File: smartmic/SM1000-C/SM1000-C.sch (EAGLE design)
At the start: 177 parts, among them CN1 HDR100-3, CN10 MJ-3523-SMT, CN11 HDR100-3, CN12 DF11-16DS, CN2 MOLEX-MINI-B-SMT, CN3 RASM712PX, CN4 RJ-45, CN5 MJ-3523-SMT, CN6 MJ-3523-SMT, CN7 MJ-3523-SMT, CN8 MJ-3523-SMT, CN9 MJ-3523-SMT, J1 JMP-2PIN, J3 JMP-2PIN, J4 JMP-2PIN, J5 JMP-2PIN, P1 TPAD50, P10 TPAD50, P11 TPAD50, P12 TPAD50, P13 TPAD50, P14 TPAD50, P15 TPAD50, P16 TPAD50, P17 TPAD50, P18 TPAD50, P19 TPAD50, P2 TPAD50, P20 TPAD50, P3 TPAD50, P4 TPAD50, P5 TPAD50, P6 TPAD50, P7 TPAD50, P8 TPAD50, P9 TPAD50, SW1 SW-BOURNS-7914S, SW2 SW-BOURNS-7914S, SW3 DPDT, SW4 SW-BOURNS-7914S, T1 SM-LP-5001, T2 SM-LP-5001, U1 STM32F405, U2 LD3985M33R, U3 STMPS2141, U4 EMIF02-USB03F2, U5 TPS54329E, U6 LMV341, U7 LMV341, U8 LM386M-1, U9 LMV341

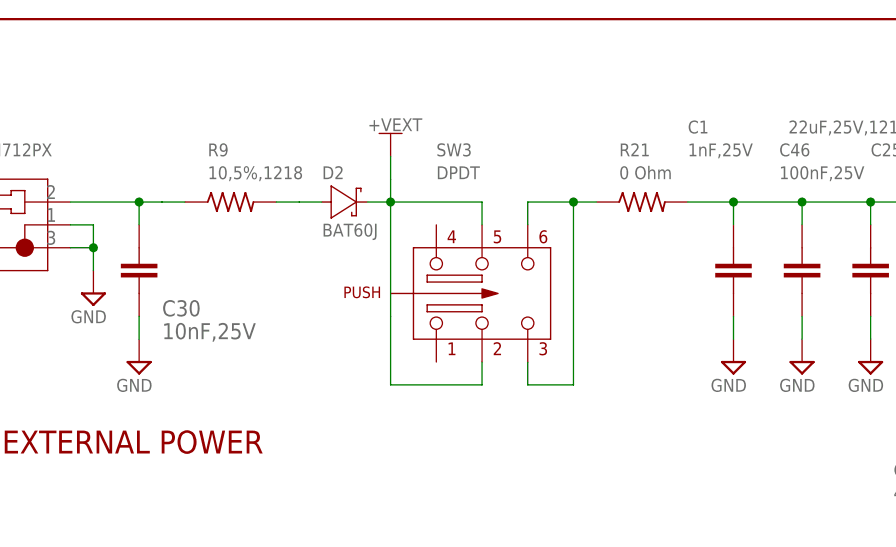
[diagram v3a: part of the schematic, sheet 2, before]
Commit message: Update Change-Log-C.txt #53 & #55  RGB 09/11/2014
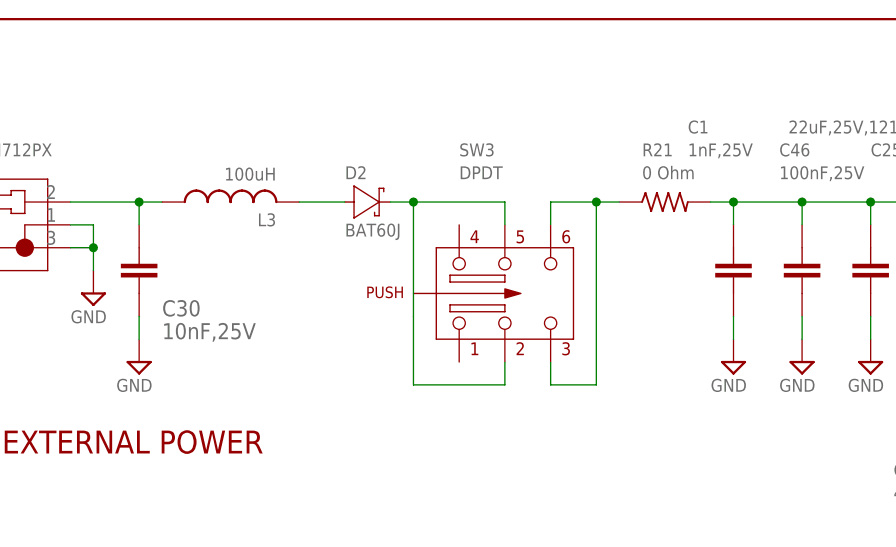
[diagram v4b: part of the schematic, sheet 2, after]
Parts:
- removed R9: 10,5%,1218, SM1000:RCL1218
- added L3: 100uH, _RoweTel:CBC3225T101MR
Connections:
- net +VEXT renamed N$15
- net N$24: now also L3.2; no longer R9.2
- net N$77: now also L3.1; no longer R9.1
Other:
- moved on the sheet: D2, R21, SW3
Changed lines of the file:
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@@
 <part name="V110" library="A-SUPPLY2" deviceset="GND" device=""/>
 <part name="U$1" library="A-SUPPLY2" deviceset="+VIN" device=""/>
-<part name="U$7" library="A-SUPPLY2" deviceset="+VEXT" device=""/>
 <part name="V71" library="A-SUPPLY2" deviceset="GND" device=""/>
 <part name="C52" library="AA-ipc-7351-capacitor" deviceset="CAPACITOR_" device="0603" value="100nF,16V"/>
@@
 <part name="C30" library="AA-ipc-7351-capacitor" deviceset="CAPACITOR_" device="0603" value="10nF,25V"/>
 <part name="V122" library="A-SUPPLY2" deviceset="GND" device=""/>
-<part name="R9" library="SM1000" deviceset="RCL1218" device="" value="10,5%,1218"/>
 <part name="R11" library="AA-ipc-7351-resistor" deviceset="RESISTOR_" device="0603" value="100,1%"/>
 <part name="R18" library="_RoweTel" deviceset="RES0805" device="" value="0 Ohm"/>
@@
 <part name="C54" library="AA-ipc-7351-capacitor" deviceset="CAPACITOR_" device="0603" value="1nF,16V"/>
 <part name="R23" library="AA-ipc-7351-resistor" deviceset="RESISTOR_" device="0603" value="10K,1%"/>
+<part name="L3" library="_RoweTel" deviceset="CBC3225T101MR" device="" value="100uH"/>
 </parts>
 <sheets>
@@
 <attribute name="VALUE" x="40.64" y="60.96" size="1.4224" layer="96" ratio="9" rot="MR270"/>
 </instance>
-<instance part="SW3" gate="G$1" x="73.66" y="248.92" smashed="yes" rot="MR0">
-<attribute name="NAME" x="68.58" y="264.16" size="1.4224" layer="95" ratio="10"/>
-<attribute name="VALUE" x="68.58" y="261.62" size="1.4224" layer="96" ratio="10"/>
+<instance part="SW3" gate="G$1" x="76.2" y="248.92" smashed="yes" rot="MR0">
+<attribute name="NAME" x="71.12" y="264.16" size="1.4224" layer="95" ratio="10"/>
+<attribute name="VALUE" x="71.12" y="261.62" size="1.4224" layer="96" ratio="10"/>
 </instance>
 <instance part="C26" gate="G$1" x="177.8" y="254" smashed="yes" rot="R270">
@@
 <attribute name="VALUE" x="106.68" y="237.998" size="1.4224" layer="96" ratio="9"/>
 </instance>
-<instance part="D2" gate="G$1" x="58.42" y="259.08" smashed="yes" rot="R180">
-<attribute name="NAME" x="55.88" y="261.62" size="1.4224" layer="95" ratio="10"/>
-<attribute name="VALUE" x="55.88" y="255.2446" size="1.4224" layer="96" ratio="10"/>
+<instance part="D2" gate="G$1" x="60.96" y="259.08" smashed="yes" rot="R180">
+<attribute name="NAME" x="58.42" y="261.62" size="1.4224" layer="95" ratio="10"/>
+<attribute name="VALUE" x="58.42" y="255.2446" size="1.4224" layer="96" ratio="10"/>
 </instance>
 <instance part="MIC1" gate="G$1" x="35.56" y="172.72" smashed="yes">
@@
 <attribute name="VALUE" x="121.92" y="267.208" size="1.4224" layer="95" ratio="9"/>
 </instance>
-<instance part="U$7" gate="G$1" x="63.5" y="266.7" smashed="yes">
-<attribute name="VALUE" x="60.96" y="266.954" size="1.4224" layer="96" ratio="9"/>
-</instance>
 <instance part="V17" gate="G$1" x="76.2" y="165.1" smashed="yes">
 <attribute name="VALUE" x="73.66" y="168.148" size="1.4224" layer="95" ratio="9"/>
@@
 <attribute name="VALUE" x="33.02" y="237.998" size="1.4224" layer="96" ratio="9"/>
 </instance>
-<instance part="R9" gate="G$1" x="45.72" y="259.08"/>
 <instance part="R11" gate="G$1" x="66.04" y="132.08" smashed="yes">
 <attribute name="NAME" x="63.5" y="133.604" size="1.4224" layer="95"/>
 <attribute name="VALUE" x="63.5" y="128.778" size="1.4224" layer="96"/>
 </instance>
-<instance part="R21" gate="G$1" x="91.44" y="259.08"/>
+<instance part="R21" gate="G$1" x="93.98" y="259.08"/>
 <instance part="R22" gate="G$1" x="27.94" y="60.96" smashed="yes" rot="R90">
 <attribute name="NAME" x="22.86" y="58.42" size="1.4224" layer="95" ratio="9" rot="R90"/>
@@
 <attribute name="VALUE" x="187.96" y="149.86" size="1.4224" layer="96" ratio="9"/>
 </instance>
+<instance part="L3" gate="G$1" x="45.72" y="259.08" smashed="yes" rot="R90">
+<attribute name="NAME" x="50.8" y="257.81" size="1.4224" layer="95" rot="R180"/>
+<attribute name="VALUE" x="50.8" y="262.89" size="1.4224" layer="96" rot="R180"/>
+</instance>
 </instances>
 <busses>
@@
 <wire x1="109.22" y1="256.54" x2="109.22" y2="259.08" width="0.1524" layer="91"/>
 <junction x="109.22" y="259.08"/>
-<wire x1="96.52" y1="259.08" x2="101.6" y2="259.08" width="0.1524" layer="91"/>
+<wire x1="99.06" y1="259.08" x2="101.6" y2="259.08" width="0.1524" layer="91"/>
 <wire x1="101.6" y1="259.08" x2="109.22" y2="259.08" width="0.1524" layer="91"/>
 <wire x1="124.46" y1="261.62" x2="124.46" y2="259.08" width="0.1524" layer="91"/>
@@
 <wire x1="35.56" y1="256.54" x2="35.56" y2="259.08" width="0.1524" layer="91"/>
 <junction x="35.56" y="259.08"/>
-<pinref part="R9" gate="G$1" pin="1"/>
-<wire x1="38.1" y1="259.08" x2="40.64" y2="259.08" width="0.1524" layer="91"/>
+<pinref part="L3" gate="G$1" pin="1"/>
 </segment>
 </net>
@@
 <segment>
 <pinref part="D2" gate="G$1" pin="A"/>
-<wire x1="53.34" y1="259.08" x2="55.88" y2="259.08" width="0.1524" layer="91"/>
-<pinref part="R9" gate="G$1" pin="2"/>
-<wire x1="50.8" y1="259.08" x2="53.34" y2="259.08" width="0.1524" layer="91"/>
+<wire x1="53.34" y1="259.08" x2="58.42" y2="259.08" width="0.1524" layer="91"/>
+<pinref part="L3" gate="G$1" pin="2"/>
 </segment>
 </net>
@@
 </segment>
 </net>
-<net name="+VEXT" class="0">
-<segment>
-<pinref part="U$7" gate="G$1" pin="+VEXT"/>
-<pinref part="SW3" gate="G$1" pin="2"/>
-<wire x1="73.66" y1="241.3" x2="73.66" y2="238.76" width="0.1524" layer="91"/>
-<wire x1="73.66" y1="238.76" x2="63.5" y2="238.76" width="0.1524" layer="91"/>
-<wire x1="63.5" y1="238.76" x2="63.5" y2="246.38" width="0.1524" layer="91"/>
-<pinref part="SW3" gate="G$1" pin="5"/>
-<wire x1="73.66" y1="256.54" x2="73.66" y2="259.08" width="0.1524" layer="91"/>
-<wire x1="63.5" y1="259.08" x2="73.66" y2="259.08" width="0.1524" layer="91"/>
-<wire x1="63.5" y1="246.38" x2="63.5" y2="259.08" width="0.1524" layer="91"/>
-<pinref part="D2" gate="G$1" pin="C"/>
-<wire x1="60.96" y1="259.08" x2="63.5" y2="259.08" width="0.1524" layer="91"/>
-<junction x="63.5" y="259.08"/>
-<wire x1="63.5" y1="259.08" x2="63.5" y2="261.62" width="0.1524" layer="91"/>
-<wire x1="63.5" y1="261.62" x2="63.5" y2="264.16" width="0.1524" layer="91"/>
-</segment>
-</net>
 <net name="N$70" class="0">
 <segment>
 <pinref part="SW3" gate="G$1" pin="3"/>
-<wire x1="78.74" y1="241.3" x2="78.74" y2="238.76" width="0.1524" layer="91"/>
-<wire x1="78.74" y1="238.76" x2="83.82" y2="238.76" width="0.1524" layer="91"/>
-<wire x1="83.82" y1="238.76" x2="83.82" y2="259.08" width="0.1524" layer="91"/>
+<wire x1="81.28" y1="241.3" x2="81.28" y2="238.76" width="0.1524" layer="91"/>
+<wire x1="81.28" y1="238.76" x2="86.36" y2="238.76" width="0.1524" layer="91"/>
+<wire x1="86.36" y1="238.76" x2="86.36" y2="259.08" width="0.1524" layer="91"/>
 <pinref part="SW3" gate="G$1" pin="6"/>
-<wire x1="78.74" y1="256.54" x2="78.74" y2="259.08" width="0.1524" layer="91"/>
-<wire x1="78.74" y1="259.08" x2="83.82" y2="259.08" width="0.1524" layer="91"/>
-<wire x1="83.82" y1="259.08" x2="86.36" y2="259.08" width="0.1524" layer="91"/>
-<junction x="83.82" y="259.08"/>
+<wire x1="81.28" y1="256.54" x2="81.28" y2="259.08" width="0.1524" layer="91"/>
+<wire x1="81.28" y1="259.08" x2="86.36" y2="259.08" width="0.1524" layer="91"/>
+<wire x1="86.36" y1="259.08" x2="88.9" y2="259.08" width="0.1524" layer="91"/>
+<junction x="86.36" y="259.08"/>
 <pinref part="R21" gate="G$1" pin="1"/>
 </segment>
@@
 </segment>
 </net>
+<net name="N$15" class="0">
+<segment>
+<pinref part="SW3" gate="G$1" pin="2"/>
+<wire x1="76.2" y1="241.3" x2="76.2" y2="238.76" width="0.1524" layer="91"/>
+<wire x1="76.2" y1="238.76" x2="66.04" y2="238.76" width="0.1524" layer="91"/>
+<wire x1="66.04" y1="238.76" x2="66.04" y2="246.38" width="0.1524" layer="91"/>
+<pinref part="SW3" gate="G$1" pin="5"/>
+<wire x1="76.2" y1="256.54" x2="76.2" y2="259.08" width="0.1524" layer="91"/>
+<wire x1="66.04" y1="259.08" x2="76.2" y2="259.08" width="0.1524" layer="91"/>
+<wire x1="66.04" y1="246.38" x2="66.04" y2="259.08" width="0.1524" layer="91"/>
+<pinref part="D2" gate="G$1" pin="C"/>
+<wire x1="63.5" y1="259.08" x2="66.04" y2="259.08" width="0.1524" layer="91"/>
+<junction x="66.04" y="259.08"/>
+</segment>
+</net>

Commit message: Changes to PCB & Schematic. Added ststus line to each Change-Log-C item to reflect current status. RGB 09/15/14
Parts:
- CN3: value RASM712PX -> RASM722PX; device _RoweTel:RASM712PX -> _RoweTel:RASM722PX
- CN6, CN8: value MJ-3523-SMT -> SJ-3524-SMT; device _RoweTel:MJ-3523-SMT -> _RoweTel:SJ-3524
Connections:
- net N$62: now also CN8.4; no longer CN8.10
- net N$75: now also CN8.3
- net SPKR: now also CN6.4; no longer CN6.10
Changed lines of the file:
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@@
 <part name="U4" library="AA-IC" deviceset="EMIF02-USB03F2" device=""/>
 <part name="CN5" library="_RoweTel" deviceset="MJ-3523-SMT" device=""/>
-<part name="CN8" library="_RoweTel" deviceset="MJ-3523-SMT" device=""/>
 <part name="L2" library="_RoweTel" deviceset="SRN6045" device="" value="4.7uH"/>
 <part name="C39" library="_RoweTel" deviceset="CAP-CHEMI-MVE-HA0" device="" value="220uF,25V"/>
@@
 <part name="V58" library="A-SUPPLY2" deviceset="GND" device=""/>
 <part name="CN9" library="_RoweTel" deviceset="MJ-3523-SMT" device=""/>
-<part name="CN6" library="_RoweTel" deviceset="MJ-3523-SMT" device=""/>
 <part name="V68" library="A-SUPPLY2" deviceset="RF" device=""/>
 <part name="CN7" library="_RoweTel" deviceset="MJ-3523-SMT" device=""/>
@@
 <part name="V83" library="A-SUPPLY2" deviceset="VDD" device=""/>
 <part name="C33" library="AA-ipc-7351-capacitor" deviceset="CAPACITOR_" device="0603" value="100nF,16V"/>
-<part name="CN3" library="_RoweTel" deviceset="RASM712PX" device=""/>
+<part name="CN3" library="_RoweTel" deviceset="RASM722PX" device=""/>
 <part name="U7" library="_RoweTel" deviceset="LMV341" device=""/>
 <part name="U6" library="_RoweTel" deviceset="LMV341" device=""/>
@@
 <part name="R23" library="AA-ipc-7351-resistor" deviceset="RESISTOR_" device="0603" value="10K,1%"/>
 <part name="L3" library="_RoweTel" deviceset="CBC3225T101MR" device="" value="100uH"/>
+<part name="CN8" library="_RoweTel" deviceset="SJ-3524" device="" value="SJ-3524-SMT"/>
+<part name="CN6" library="_RoweTel" deviceset="SJ-3524" device="" value="SJ-3524-SMT"/>
 </parts>
 <sheets>
@@
 <attribute name="VALUE" x="15.24" y="137.16" size="1.778" layer="95" ratio="10" rot="MR180"/>
 </instance>
-<instance part="CN8" gate="G$1" x="127" y="53.34" smashed="yes" rot="R180">
-<attribute name="NAME" x="142.24" y="43.18" size="1.778" layer="95" ratio="10" rot="R180"/>
-<attribute name="VALUE" x="142.24" y="60.96" size="1.778" layer="95" ratio="10" rot="R180"/>
-</instance>
 <instance part="L2" gate="G$1" x="187.96" y="246.38" smashed="yes" rot="R90">
 <attribute name="NAME" x="193.04" y="245.11" size="1.4224" layer="95" rot="R180"/>
@@
 <attribute name="VALUE" x="73.66" y="22.098" size="1.4224" layer="96" ratio="9"/>
 </instance>
-<instance part="V66" gate="GND" x="116.84" y="40.64" smashed="yes">
-<attribute name="VALUE" x="114.3" y="37.338" size="1.4224" layer="96" ratio="9"/>
+<instance part="V66" gate="GND" x="119.38" y="35.56" smashed="yes">
+<attribute name="VALUE" x="116.84" y="32.258" size="1.4224" layer="96" ratio="9"/>
 </instance>
 <instance part="V67" gate="GND" x="53.34" y="48.26" smashed="yes">
@@
 <attribute name="VALUE" x="307.34" y="58.42" size="1.778" layer="95" ratio="10" rot="R180"/>
 </instance>
-<instance part="CN6" gate="G$1" x="292.1" y="132.08" smashed="yes" rot="R180">
-<attribute name="NAME" x="289.56" y="137.16" size="1.778" layer="95" ratio="10"/>
-<attribute name="VALUE" x="297.18" y="137.16" size="1.778" layer="95" ratio="10"/>
-</instance>
 <instance part="V68" gate="G$1" x="264.16" y="119.38" smashed="yes">
 <attribute name="VALUE" x="261.9375" y="116.84" size="1.4224" layer="96" ratio="12"/>
@@
 <attribute name="VALUE" x="50.8" y="262.89" size="1.4224" layer="96" rot="R180"/>
 </instance>
+<instance part="CN8" gate="G$1" x="124.46" y="50.8" rot="R180"/>
+<instance part="CN6" gate="G$1" x="292.1" y="129.54" rot="R180"/>
 </instances>
 <busses>
@@
 </segment>
 <segment>
-<pinref part="CN8" gate="G$1" pin="1"/>
-<wire x1="119.38" y1="45.72" x2="116.84" y2="45.72" width="0.1524" layer="91"/>
-<wire x1="116.84" y1="45.72" x2="116.84" y2="43.18" width="0.1524" layer="91"/>
+<wire x1="119.38" y1="40.64" x2="119.38" y2="38.1" width="0.1524" layer="91"/>
 <pinref part="V66" gate="GND" pin="GND"/>
+<pinref part="CN8" gate="G$1" pin="1"/>
 </segment>
 <segment>
@@
 <net name="SPKR" class="0">
 <segment>
-<pinref part="CN6" gate="G$1" pin="10"/>
 <wire x1="284.48" y1="129.54" x2="261.62" y2="129.54" width="0.1524" layer="91"/>
 <wire x1="261.62" y1="147.32" x2="261.62" y2="129.54" width="0.1524" layer="91"/>
@@
 <pinref part="C43" gate="G$1" pin="1"/>
 <wire x1="243.84" y1="162.56" x2="243.84" y2="160.02" width="0.1524" layer="91"/>
+<pinref part="CN6" gate="G$1" pin="4"/>
+<wire x1="284.48" y1="129.54" x2="287.02" y2="129.54" width="0.1524" layer="91"/>
 </segment>
 </net>
@@
 </segment>
 <segment>
-<pinref part="CN6" gate="G$1" pin="1"/>
 <wire x1="251.46" y1="124.46" x2="264.16" y2="124.46" width="0.1524" layer="91"/>
-<wire x1="264.16" y1="124.46" x2="284.48" y2="124.46" width="0.1524" layer="91"/>
+<wire x1="264.16" y1="124.46" x2="271.78" y2="124.46" width="0.1524" layer="91"/>
 <wire x1="264.16" y1="124.46" x2="264.16" y2="121.92" width="0.1524" layer="91"/>
 <junction x="264.16" y="124.46"/>
 <pinref part="V68" gate="G$1" pin="RF"/>
 <pinref part="T1" gate="G$1" pin="4"/>
+<wire x1="271.78" y1="124.46" x2="271.78" y2="119.38" width="0.1524" layer="91"/>
+<pinref part="CN6" gate="G$1" pin="1"/>
+<wire x1="271.78" y1="119.38" x2="287.02" y2="119.38" width="0.1524" layer="91"/>
 </segment>
 <segment>
@@
 <segment>
 <pinref part="FB1" gate="G$1" pin="2"/>
-<pinref part="CN6" gate="G$1" pin="2"/>
 <wire x1="281.94" y1="134.62" x2="284.48" y2="134.62" width="0.1524" layer="91"/>
+<pinref part="CN6" gate="G$1" pin="2"/>
+<wire x1="284.48" y1="134.62" x2="287.02" y2="134.62" width="0.1524" layer="91"/>
 </segment>
 </net>
@@
 <segment>
 <pinref part="FB3" gate="G$1" pin="2"/>
+<wire x1="106.68" y1="55.88" x2="116.84" y2="55.88" width="0.1524" layer="91"/>
+<pinref part="CN8" gate="G$1" pin="3"/>
+<wire x1="116.84" y1="55.88" x2="119.38" y2="55.88" width="0.1524" layer="91"/>
+<wire x1="119.38" y1="45.72" x2="116.84" y2="45.72" width="0.1524" layer="91"/>
+<wire x1="116.84" y1="45.72" x2="116.84" y2="55.88" width="0.1524" layer="91"/>
+<junction x="116.84" y="55.88"/>
 <pinref part="CN8" gate="G$1" pin="2"/>
-<wire x1="106.68" y1="55.88" x2="119.38" y2="55.88" width="0.1524" layer="91"/>
 </segment>
 </net>
@@
 <net name="N$62" class="0">
 <segment>
-<pinref part="CN8" gate="G$1" pin="10"/>
 <pinref part="J4" gate="G$1" pin="1"/>
 <wire x1="119.38" y1="50.8" x2="106.68" y2="50.8" width="0.1524" layer="91"/>
 <wire x1="106.68" y1="50.8" x2="106.68" y2="48.26" width="0.1524" layer="91"/>
+<pinref part="CN8" gate="G$1" pin="4"/>
 </segment>
 </net>

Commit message: Update Eagle Files  RGB 9/24/14
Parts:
- added P21, P22, P23, P24: PAD070-035, _Coherix:PAD070-035
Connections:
- new net AVDD: C22.1, C32.1, C35.1, C41.1, C42.1, C50.1, J3.2, P24.1, R38.2, R44.2, U6.!SHDN!, U6.V+, U7.!SHDN!, U7.V+, U9.!SHDN!
- new net AVSS: C10.2, C11.2, C12.2, C13.2, C22.2, C23.2, C32.2, C34.2, C35.2, C41.2, C42.2, C50.2, CN5.1, CN8.1, J4.2, MIC1.2, P23.1, R22.1, R40.2, R45.2, R46.1, R50.2, R52.1, T1.3, T2.3, U1B.VSSA, U6.GND, U7.GND, U8.-IN, U8.GND, U9.GND
- net GND: now also P22.1; no longer C10.2, C11.2, C12.2, C13.2, C22.2, C23.2, C32.2, C34.2, C35.2, C41.2, C42.2, C50.2, CN5.1, CN8.1, J4.2, MIC1.2, R22.1, R40.2, R45.2, R46.1, R50.2, R52.1, T1.3, T2.3, U1B.VSSA, U6.GND, U7.GND, U8.-IN, U8.GND, U9.GND
- net VDD: now also P21.1; no longer C22.1, C32.1, C35.1, C41.1, C42.1, C50.1, J3.2, R38.2, R44.2, U6.!SHDN!, U6.V+, U7.!SHDN!, U7.V+, U9.!SHDN!
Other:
- moved on the sheet: C15
